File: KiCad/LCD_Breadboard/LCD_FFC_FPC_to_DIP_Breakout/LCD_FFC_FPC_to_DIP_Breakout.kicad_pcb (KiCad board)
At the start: 2 copper layers, 70 x 35 mm, 7 parts, among them J1_Even1 Even_2_to_40, J1_Odd1 Odd_1_to_39

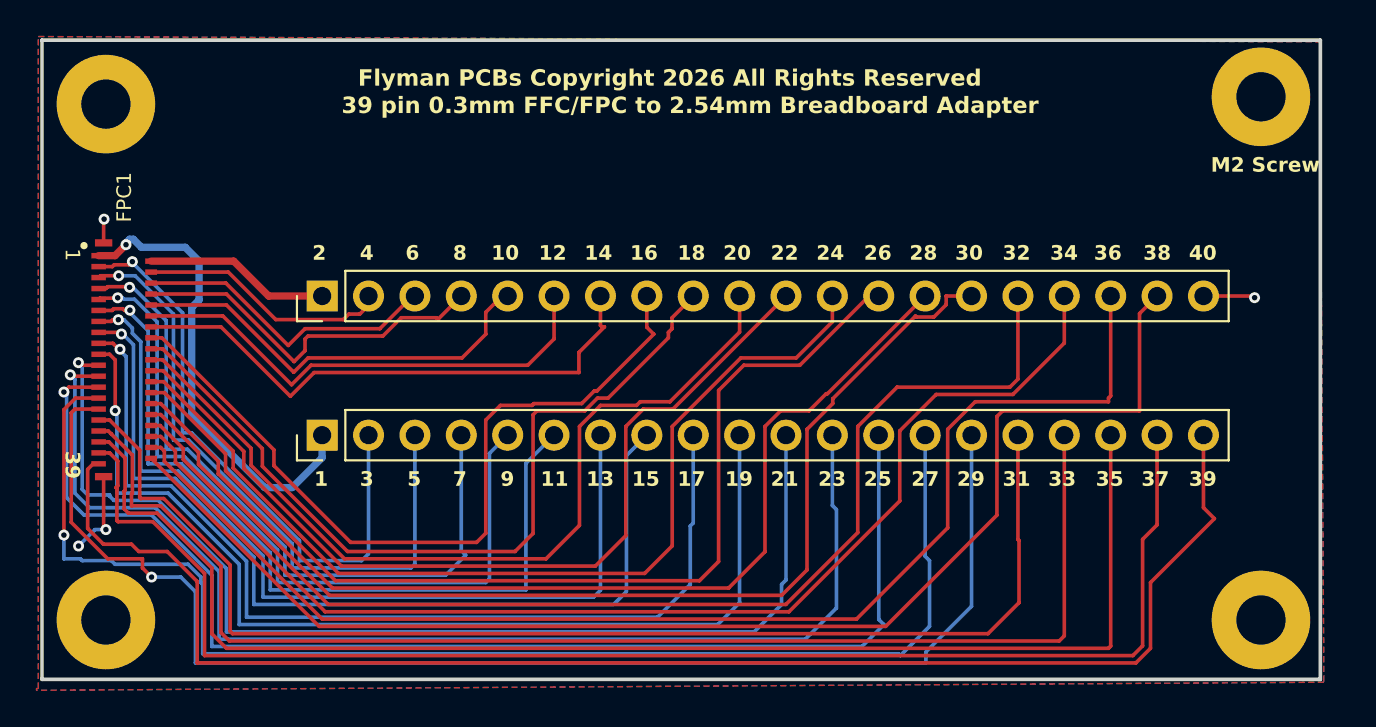
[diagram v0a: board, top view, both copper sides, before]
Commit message: Bring full design history into git + repo cleanup
- Add never-tracked KiCad projects: PelletPirate_V3, PelletPirate_V4, ESP_Breadboard (+V2_Quilter), FPC_for_PCB_to_LCD RevC-RevH flex designs
- Add esp_breadboard_test_fw source (build/ ignored)
- Remove stale root PNGs/PDFs and old V2 backup zips/libs (moves detected as renames)
- Ignore >100MB local archives (gen_channels.zip, PelletPirate_V3.zip, BACKUP_ZIPS/) and S3 build artifacts

Co-Authored-By: Claude Fable 5 <noreply@anthropic.com>
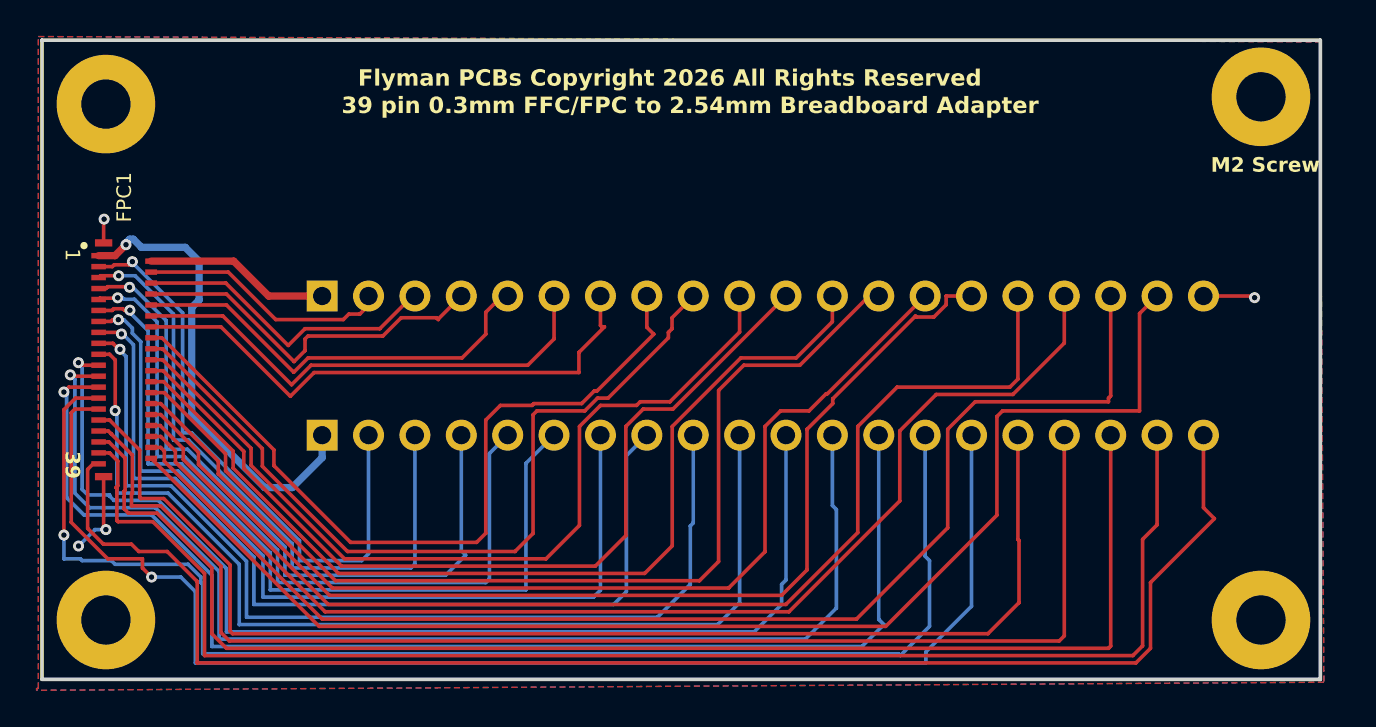
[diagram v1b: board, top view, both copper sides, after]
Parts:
- J1_Even1, J1_Odd1: moved to B.Cu
- turned J1_Even1 to -90 degrees
- turned J1_Odd1 to -90 degrees
